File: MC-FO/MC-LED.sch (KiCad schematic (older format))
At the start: 11 parts, among them U181 TPS3703A5330DSER, U182 74ACT08SCX, U183 TPS3703A5500DSER, U184 74LVC1G07QDCKTQ1

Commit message: DSP schem, FO schem, and FO layout changes
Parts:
- R181: value 10 K -> 10K
- R182: renamed from R183; value 10 K -> 10K
- R183: renamed from R182; value 500 Ohm -> 500R
- R184: renamed from R19; value 10 K -> 10K
- renumbered U183 to U182, U182 to U183
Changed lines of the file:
@@
 Power Indicator LED CKT
 $Comp
-L Device:R_US R182
+L Device:R_US R183
 U 1 1 61706570
 P 3850 4650
-F 0 "R182" H 3700 4550 50  0000 C CNN
-F 1 "500 Ohm" H 3600 4650 50  0000 C CNN
+F 0 "R183" H 3700 4550 50  0000 C CNN
+F 1 "500R" H 3600 4650 50  0000 C CNN
 F 2 "Resistor_SMD:R_0603_1608Metric" V 3890 4640 50  0001 C CNN
 F 3 "~" H 3850 4650 50  0001 C CNN
@@
 5V
 $Comp
-L Existing_IC_Models:74ACT08SCX U182
+L Existing_IC_Models:74ACT08SCX U183
 U 1 1 6176E3CF
 P 3000 3550
-F 0 "U182" H 3000 3665 50  0000 C CNN
+F 0 "U183" H 3000 3665 50  0000 C CNN
 F 1 "74ACT08SCX" H 3000 3574 50  0000 C CNN
 F 2 "Package_SO:SOIC-14_3.9x8.7mm_P1.27mm" H 3000 3550 50  0001 C CNN
@@
 $EndComp
 $Comp
-L Existing_IC_Models:TPS3703A5500DSER U183
+L Existing_IC_Models:TPS3703A5500DSER U182
 U 1 1 6177F576
 P 4250 2250
-F 0 "U183" H 4250 2215 50  0000 C CNN
+F 0 "U182" H 4250 2215 50  0000 C CNN
 F 1 "TPS3703A5500DSER" H 4250 2124 50  0000 C CNN
 F 2 "Package_SON:WSON-6_1.5x1.5mm_P0.5mm" H 4250 2250 50  0001 C CNN
@@
 P 2900 2700
 F 0 "R181" H 2968 2746 50  0000 L CNN
-F 1 "10 K" H 2968 2655 50  0000 L CNN
+F 1 "10K" H 2968 2655 50  0000 L CNN
 F 2 "Resistor_SMD:R_0603_1608Metric" H 2900 2700 50  0001 C CNN
 F 3 "~" H 2900 2700 50  0001 C CNN
@@
 $EndComp
 $Comp
-L Device:R_Small_US R183
+L Device:R_Small_US R182
 U 1 1 617C3F20
 P 5200 2550
-F 0 "R183" H 5268 2596 50  0000 L CNN
-F 1 "10 K" H 5268 2505 50  0000 L CNN
+F 0 "R182" H 5268 2596 50  0000 L CNN
+F 1 "10K" H 5268 2505 50  0000 L CNN
 F 2 "Resistor_SMD:R_0603_1608Metric" H 5200 2550 50  0001 C CNN
 F 3 "~" H 5200 2550 50  0001 C CNN
@@
 Wire Wire Line
 	6350 4100 7050 4100
-$Comp
-L Device:R_Small_US R19
-U 1 1 6182FD38
-P 6350 3500
-F 0 "R19" H 6418 3546 50  0000 L CNN
-F 1 "10 K" H 6418 3455 50  0000 L CNN
-F 2 "Resistor_SMD:R_0603_1608Metric" H 6350 3500 50  0001 C CNN
-F 3 "~" H 6350 3500 50  0001 C CNN
-	1    6350 3500
-	1    0    0    -1
-$EndComp
 Text HLabel 6450 3100 2    50   Input ~ 0
 3V3
@@
 	0    -1   -1   0
 $EndComp
+$Comp
+L Device:R_Small_US R184
+U 1 1 6182FD38
+P 6350 3500
+F 0 "R184" H 6418 3546 50  0000 L CNN
+F 1 "10K" H 6418 3455 50  0000 L CNN
+F 2 "Resistor_SMD:R_0603_1608Metric" H 6350 3500 50  0001 C CNN
+F 3 "~" H 6350 3500 50  0001 C CNN
+	1    6350 3500
+	1    0    0    -1
+$EndComp
 $EndSCHEMATC

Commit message: Changed V-monitor circuit, V-reg circuit, finished detectors
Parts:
- removed U181: TPS3703A5330DSER, Package_SON:WSON-6_1.5x1.5mm_P0.5mm, symbol Existing_IC_Models:TPS3703A5330DSER
- removed U182: TPS3703A5500DSER, Package_SON:WSON-6_1.5x1.5mm_P0.5mm, symbol Existing_IC_Models:TPS3703A5500DSER
- added U181: BU4831F-TR, SOT130P210X105-4N, symbol BU4831F-TR:BU4831F-TR
- added U182: BU4847F-TR, SOT130P210X105-4N, symbol BU4847F-TR:BU4847F-TR
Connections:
- wire segments 87 -> 48
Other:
- moved on the sheet: C181, C182, R181, R182, U184

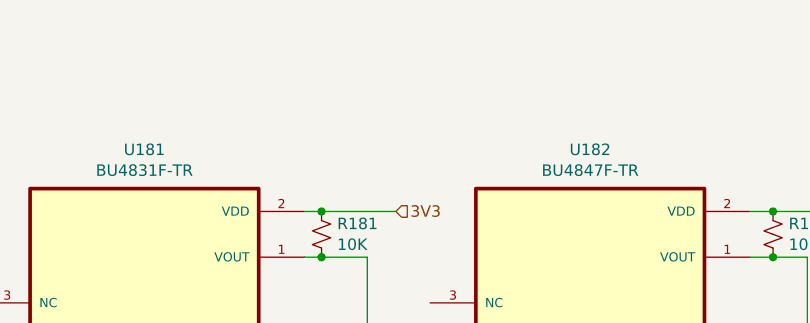
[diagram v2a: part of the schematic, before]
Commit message: updated top level of schematic with "to test" and "to do" notes
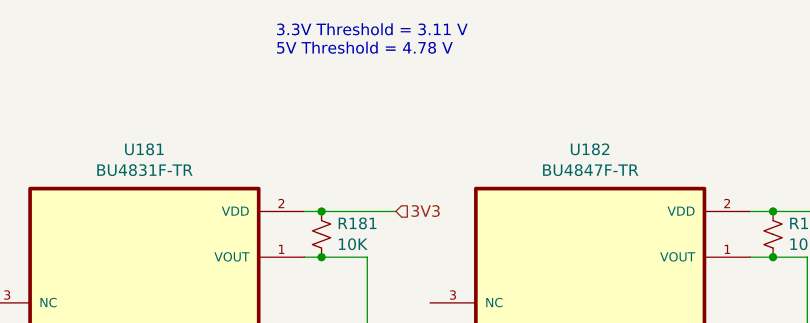
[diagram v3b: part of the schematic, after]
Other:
- note added: "3.3V Threshold = 3.11 V\n5V Threshold = 4.78 V"
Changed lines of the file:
@@
 Wire Wire Line
 	4475 3175 4475 3075
+Text Notes 3200 1400 0    50   ~ 0
+3.3V Threshold = 3.11 V\n5V Threshold = 4.78 V
 $EndSCHEMATC

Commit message: Add files via upload
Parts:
- added TP17, TP18, TP19: TestPoint, TestPoint:TestPoint_Pad_D2.0mm, symbol Connector:TestPoint
- U181, U182: footprint SOT130P210X105-4N -> Package_SO:SOP-4_3.8x4.1mm_P2.54mm
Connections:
- net 5V: no longer U183.4 (A1)
- net RESET_FO: now also U183.4 (A1), TP19.1
- net at R183.2, U183.3 (Y0), U183.8 (Y3): no longer U183.6 (Y1)
- net at U183.10 (A3), U183.11 (Y2), U183.2 (B0)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: no longer U183.5 (B1)
- net at R182.2, U182.1 (VOUT), U183.12 (B2): now also TP18.1
- net at R181.2, U181.1 (VOUT), U183.13 (A2): now also TP17.1
- new net SAFE_STATE_FLAG: U183.5 (B1), U183.6 (Y1)
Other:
- note added: "a high RESET_FO shows there are no voltage issues with FO on FO GD card. \na low RESET_FO or low Safe_state = turn off"
- note removed: "Delete status led /gpio signal"
- moved on the sheet: D181, R183
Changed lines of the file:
@@
 $Descr A4 11693 8268
 encoding utf-8
-Sheet 8 10
+Sheet 7 11
 Title ""
 Date ""
@@
 L Device:R_US R183
 U 1 1 61706570
-P 3850 4650
-F 0 "R183" H 3700 4550 50  0000 C CNN
-F 1 "500R" H 3600 4650 50  0000 C CNN
-F 2 "Resistor_SMD:R_0603_1608Metric" V 3890 4640 50  0001 C CNN
-F 3 "~" H 3850 4650 50  0001 C CNN
-	1    3850 4650
+P 3850 4500
+F 0 "R183" H 3700 4400 50  0000 C CNN
+F 1 "500R" H 3600 4500 50  0000 C CNN
+F 2 "Resistor_SMD:R_0603_1608Metric" V 3890 4490 50  0001 C CNN
+F 3 "~" H 3850 4500 50  0001 C CNN
+	1    3850 4500
 	-1   0    0    1
 $EndComp
-Text HLabel 4900 5500 3    50   Input ~ 0
-GND
-Wire Wire Line
-	3850 4300 3850 4500
+Text HLabel 4900 5250 3    50   Input ~ 0
+GND
+Wire Wire Line
+	3850 4300 3850 4350
 Wire Wire Line
 	2600 3900 2350 3900
 Wire Wire Line
-	2350 3900 2350 4200
-Wire Wire Line
-	2350 4200 2600 4200
-Wire Wire Line
-	2350 4200 2350 4550
-Wire Wire Line
 	2350 4550 3500 4550
 Wire Wire Line
@@
 Wire Wire Line
 	3500 4300 3400 4300
-Connection ~ 2350 4200
 Wire Wire Line
 	3500 4300 3850 4300
@@
 Wire Wire Line
 	3650 4700 2250 4700
-Wire Wire Line
-	2250 4700 2250 4100
 Connection ~ 3650 4100
-Wire Wire Line
-	2250 4100 2600 4100
 Text Notes 4050 7350 2    50   ~ 0
 add comparatorson both and logically AND together for LED on power status\n\n\n (windowed comparators or voltage supervisors)
-Text Notes 7700 4700 0    50   ~ 0
-Delete status led /gpio signal
 Text Notes 5800 2700 0    50   ~ 0
 if one or the other is not working pull the global reset down
-Text Notes 5900 5100 0    50   ~ 0
+Text Notes 6650 4475 0    50   ~ 0
 74LVC1G07: should be an open drain buffer\n
 Wire Wire Line
@@
 Connection ~ 6350 4100
 Wire Wire Line
-	6350 4100 7050 4100
+	6350 4100 6475 4100
 Text HLabel 6450 3100 2    50   Input ~ 0
 3V3
@@
 Wire Wire Line
 	6350 3600 6350 4100
-Text HLabel 7050 4100 2    50   Output ~ 0
-RESET_FO
 $Comp
 L Existing_IC_Models:74LVC1G07QDCKTQ1 U184
@@
 Connection ~ 6350 3100
 Wire Wire Line
-	5875 5400 4900 5400
-Wire Wire Line
-	4900 5400 4900 5500
-Wire Wire Line
-	5875 4200 5875 5400
-Wire Wire Line
-	3850 4800 3850 4900
-Wire Wire Line
-	3850 5200 3850 5400
-Wire Wire Line
-	3850 5400 4900 5400
-Connection ~ 4900 5400
+	5875 5150 4900 5150
+Wire Wire Line
+	4900 5150 4900 5250
+Wire Wire Line
+	5875 4200 5875 5150
+Wire Wire Line
+	3850 4650 3850 4750
+Wire Wire Line
+	3850 5050 3850 5150
+Wire Wire Line
+	3850 5150 4900 5150
+Connection ~ 4900 5150
 Wire Wire Line
 	3650 4100 5575 4100
-Text Notes 6150 5200 0    50   ~ 0
+Text Notes 6900 4725 0    50   ~ 0
 out of stock -- had to improvise\n
 $Comp
 L Existing_IC_Models:WP1503CB_GD D181
 U 1 1 6185A99A
-P 3750 5050
-F 0 "D181" V 3789 4832 50  0000 R CNN
-F 1 "WP1503CB_GD" V 3698 4832 50  0000 R CNN
-F 2 "Footprints_MC-FO:WP1503CBGD" H 3750 5150 50  0001 C CNN
-F 3 "" H 3750 5150 50  0001 C CNN
-	1    3750 5050
+P 3750 4900
+F 0 "D181" V 3789 4682 50  0000 R CNN
+F 1 "WP1503CB_GD" V 3698 4682 50  0000 R CNN
+F 2 "Footprints_MC-FO:WP1503CBGD" H 3750 5000 50  0001 C CNN
+F 3 "" H 3750 5000 50  0001 C CNN
+	1    3750 4900
 	0    -1   -1   0
 $EndComp
@@
 Text HLabel 2600 4300 0    50   Input ~ 0
 GND
-Connection ~ 2250 4100
-Wire Wire Line
-	2250 4100 2250 3800
 Wire Wire Line
 	2250 3800 2600 3800
@@
 Text HLabel 2600 3700 0    50   Input ~ 0
 5V
-Text HLabel 2600 4000 0    50   Input ~ 0
-5V
 Text HLabel 3400 4200 2    50   Input ~ 0
 5V
@@
 F 0 "U182" H 4575 2945 50  0000 C CNN
 F 1 "BU4847F-TR" H 4575 2854 50  0000 C CNN
-F 2 "SOT130P210X105-4N" H 4575 2375 50  0001 L BNN
+F 2 "Package_SO:SOP-4_3.8x4.1mm_P2.54mm" H 4575 2375 50  0001 L BNN
 F 3 "" H 4575 2375 50  0001 L BNN
 F 4 "Rohm" H 4575 2375 50  0001 L BNN "Manufacturer"
@@
 F 0 "U181" H 2625 2945 50  0000 C CNN
 F 1 "BU4831F-TR" H 2625 2854 50  0000 C CNN
-F 2 "SOT130P210X105-4N" H 2625 2375 50  0001 L BNN
+F 2 "Package_SO:SOP-4_3.8x4.1mm_P2.54mm" H 2625 2375 50  0001 L BNN
 F 3 "" H 2625 2375 50  0001 L BNN
 F 4 "Rohm" H 2625 2375 50  0001 L BNN "Manufacturer"
@@
 	3600 2275 3400 2275
 Wire Wire Line
-	5525 3900 5525 2275
+	5525 3900 5525 2900
 Wire Wire Line
 	5525 2275 5375 2275
@@
 	3400 2075 3725 2075
 Wire Wire Line
-	3600 3800 3600 2275
+	3600 3800 3600 2925
 Text HLabel 4025 3375 0    50   Input ~ 0
 GND
@@
 Text Notes 3200 1400 0    50   ~ 0
 3.3V Threshold = 3.11 V\n5V Threshold = 4.78 V
+Wire Wire Line
+	2350 3900 2350 4550
+Wire Wire Line
+	2250 3800 2250 4700
+Wire Wire Line
+	6475 4100 6475 5275
+Wire Wire Line
+	6475 5550 1775 5550
+Wire Wire Line
+	1775 5550 1775 4000
+Wire Wire Line
+	1775 4000 2600 4000
+Text Label 1775 4000 0    50   ~ 0
+RESET_FO
+Text HLabel 1475 4200 0    50   BiDi ~ 0
+SAFE_STATE_FLAG
+Wire Wire Line
+	1475 4200 1975 4200
+Wire Wire Line
+	2600 4100 1975 4100
+Wire Wire Line
+	1975 4100 1975 4200
+Connection ~ 1975 4200
+Wire Wire Line
+	1975 4200 2600 4200
+Text Notes 7100 900  0    50   ~ 0
+a high RESET_FO shows there are no voltage issues with FO on FO GD card. \na low RESET_FO or low Safe_state = turn off
+Text Label 6450 4100 0    50   ~ 0
+RESET_FO
+$Comp
+L Connector:TestPoint TP19
+U 1 1 623DE1C7
+P 6475 5275
+F 0 "TP19" V 6429 5463 50  0000 L CNN
+F 1 "TestPoint" V 6520 5463 50  0000 L CNN
+F 2 "TestPoint:TestPoint_Pad_D2.0mm" H 6675 5275 50  0001 C CNN
+F 3 "~" H 6675 5275 50  0001 C CNN
+	1    6475 5275
+	0    1    1    0
+$EndComp
+Connection ~ 6475 5275
+Wire Wire Line
+	6475 5275 6475 5550
+$Comp
+L Connector:TestPoint TP17
+U 1 1 623DFD90
+P 3600 2925
+F 0 "TP17" V 3554 3113 50  0000 L CNN
+F 1 "TestPoint" V 3645 3113 50  0000 L CNN
+F 2 "TestPoint:TestPoint_Pad_D2.0mm" H 3800 2925 50  0001 C CNN
+F 3 "~" H 3800 2925 50  0001 C CNN
+	1    3600 2925
+	0    1    1    0
+$EndComp
+Connection ~ 3600 2925
+Wire Wire Line
+	3600 2925 3600 2275
+$Comp
+L Connector:TestPoint TP18
+U 1 1 623E05CE
+P 5525 2900
+F 0 "TP18" V 5479 3088 50  0000 L CNN
+F 1 "TestPoint" V 5570 3088 50  0000 L CNN
+F 2 "TestPoint:TestPoint_Pad_D2.0mm" H 5725 2900 50  0001 C CNN
+F 3 "~" H 5725 2900 50  0001 C CNN
+	1    5525 2900
+	0    1    1    0
+$EndComp
+Connection ~ 5525 2900
+Wire Wire Line
+	5525 2900 5525 2275
 $EndSCHEMATC

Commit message: updating SAFE_STATE_FLAG and EMITTER_ENABLE
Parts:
- removed D181: WP1503CB_GD, Footprints_MC-FO:WP1503CBGD, symbol Existing_IC_Models:WP1503CB_GD
- removed R183: 500R, Resistor_SMD:R_0603_1608Metric, symbol Device:R_US
- removed TP19: TestPoint, TestPoint:TestPoint_Pad_D2.0mm, symbol Connector:TestPoint
- added D?: WP1503CB_GD, Footprints_MC-FO:WP1503CBGD, symbol Existing_IC_Models:WP1503CB_GD
- added R?: 500R, Resistor_SMD:R_0603_1608Metric, symbol Device:R_US
- added R?: 10K, Resistor_SMD:R_0603_1608Metric, symbol Device:R_Small_US
- added TP?: TestPoint, TestPoint:TestPoint_Pad_D2.0mm, symbol Connector:TestPoint
- added U?: 74LVC1G07QDCKTQ1, Package_TO_SOT_SMD:SOT-353_SC-70-5, symbol Existing_IC_Models:74LVC1G07QDCKTQ1
- added U?: 74LVCE1G08W5-7, symbol MC-FO:74LVCE1G08W5-7
- U181: symbol BU4831F-TR:BU4831F-TR -> MC-FO:BU4831F-TR
- U182: symbol BU4847F-TR:BU4847F-TR -> MC-FO:BU4847F-TR
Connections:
- net labels added: ~RESET_FO~, ~SAFE_STATE_FLAG~
- net labels removed: RESET_FO, SAFE_STATE_FLAG
- wire segments 55 -> 67
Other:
- note added: "Safe_state_flag is like a global reset to connector and to\n all transcievers. pulled low if any voltage issues on this \ncard or any other card. can also be pulled low by dsp"
- note added: "a high ~RESET_FO~ shows there are no voltage issues with FO on FO GD card. \na low RESET_FO or low Safe_state = turn off"
- note removed: "a high RESET_FO shows there are no voltage issues with FO on FO GD card. \na low RESET_FO or low Safe_state = turn off"
- note removed: "out of stock -- had to improvise\n"
- note removed: "reset to connector and to all transcievers"
- moved on the sheet: C181, C182, R181, R182, R184, TP17, TP18, U183, U184

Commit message: schematic changes--> layout rev
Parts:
- removed R?: 10K, Resistor_SMD:R_0603_1608Metric, symbol Device:R_Small_US
- removed U183: 74ACT08SCX, Package_SO:SOIC-14_3.9x8.7mm_P1.27mm, symbol Existing_IC_Models:74ACT08SCX
- removed U?: 74LVC1G07QDCKTQ1, Package_TO_SOT_SMD:SOT-353_SC-70-5, symbol Existing_IC_Models:74LVC1G07QDCKTQ1
- U181: renamed from U184; footprint Package_TO_SOT_SMD:SOT-353_SC-70-5 -> Package_TO_SOT_SMD:SOT-353_SC-70-5_Handsoldering
- U182: renamed from U?; footprint (none) -> Package_TO_SOT_SMD:SOT-23-5_HandSoldering
- gave numbers to parts that had none: 3
- renumbered C182 to C181, C181 to C182, R184 to R182, R181 to R184, R182 to R185, TP17 to TP182, TP18 to TP183, U181 to U183, U182 to U184
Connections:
- net labels removed: ~RESET_FO~
- wire segments 67 -> 36
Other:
- note removed: "a high ~RESET_FO~ shows there are no voltage issues with FO on FO GD card. \na low RESET_FO or low Safe_state = turn off"
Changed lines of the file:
@@
 Text HLabel 3125 4125 0    50   Input ~ 0
 GND
-Wire Wire Line
-	4975 10150 4725 10150
-Wire Wire Line
-	4725 10800 5875 10800
-Wire Wire Line
-	5875 10800 5875 10550
-Wire Wire Line
-	5875 10550 5775 10550
-Wire Wire Line
-	5875 10550 6225 10550
-Connection ~ 5875 10550
-Wire Wire Line
-	6025 10250 6025 10350
-Wire Wire Line
-	5775 10250 6025 10250
-Wire Wire Line
-	5775 10350 6025 10350
-Wire Wire Line
-	6025 10350 6025 10950
-Wire Wire Line
-	6025 10950 4625 10950
-Connection ~ 6025 10350
 Text Notes 4050 7350 2    50   ~ 0
 add comparatorson both and logically AND together for LED on power status\n\n\n (windowed comparators or voltage supervisors)
@@
 	2825 2925 2825 3225
 $Comp
-L Existing_IC_Models:74LVC1G07QDCKTQ1 U184
+L Existing_IC_Models:74LVC1G07QDCKTQ1 U181
 U 1 1 617E8424
 P 3125 3925
-F 0 "U184" H 2975 4175 50  0000 C CNN
+F 0 "U181" H 2975 4175 50  0000 C CNN
 F 1 "74LVC1G07QDCKTQ1" H 2725 4075 50  0000 C CNN
-F 2 "Package_TO_SOT_SMD:SOT-353_SC-70-5" H 3125 3925 50  0001 C CNN
-F 3 "http://www.ti.com/lit/sg/scyt129e/scyt129e.pdf" H 3125 3925 50  0001 C CNN
+F 2 "Package_TO_SOT_SMD:SOT-353_SC-70-5_Handsoldering" H 3125 3925 50  0001 C CNN
+F 3 "https://www.ti.com/lit/ds/symlink/sn74lvc1g07-q1.pdf?HQS=dis-mous-null-mousermode-dsf-pf-null-wwe&ts=1646082303416&ref_url=https%253A%252F%252Fwww.mouser.com%252F" H 3125 3925 50  0001 C CNN
 	1    3125 3925
 	-1   0    0    -1
@@
 Wire Wire Line
 	3125 4025 3125 4125
-Wire Wire Line
-	6025 10350 7950 10350
-$Comp
-L Device:R_Small_US R184
+$Comp
+L Device:R_Small_US R182
 U 1 1 6182FD38
 P 2825 3325
-F 0 "R184" H 2893 3371 50  0000 L CNN
+F 0 "R182" H 2893 3371 50  0000 L CNN
 F 1 "10K" H 2893 3280 50  0000 L CNN
 F 2 "Resistor_SMD:R_0603_1608Metric" H 2825 3325 50  0001 C CNN
@@
 	-1   0    0    -1
 $EndComp
-Text HLabel 4975 10550 0    50   Input ~ 0
-GND
-Wire Wire Line
-	4625 10050 4975 10050
 Text HLabel 5825 3075 2    50   Input ~ 0
 GND
 $Comp
-L Device:R_Small_US R182
+L Device:R_Small_US R185
 U 1 1 617C3F20
 P 7875 2575
-F 0 "R182" H 7943 2621 50  0000 L CNN
+F 0 "R185" H 7943 2621 50  0000 L CNN
 F 1 "10K" H 7943 2530 50  0000 L CNN
 F 2 "Resistor_SMD:R_0603_1608Metric" H 7875 2575 50  0001 C CNN
@@
 $EndComp
 $Comp
-L Device:R_Small_US R181
+L Device:R_Small_US R184
 U 1 1 617C2D42
 P 6100 2575
-F 0 "R181" H 6168 2621 50  0000 L CNN
+F 0 "R184" H 6168 2621 50  0000 L CNN
 F 1 "10K" H 6168 2530 50  0000 L CNN
 F 2 "Resistor_SMD:R_0603_1608Metric" H 6100 2575 50  0001 C CNN
@@
 5V
 $Comp
-L Device:C_Small C181
+L Device:C_Small C182
 U 1 1 617CFF8B
 P 2600 2125
-F 0 "C181" H 2692 2171 50  0000 L CNN
+F 0 "C182" H 2692 2171 50  0000 L CNN
 F 1 "1 uF or unpop" H 2692 2080 50  0000 L CNN
 F 2 "Capacitor_SMD:C_0603_1608Metric" H 2600 2125 50  0001 C CNN
@@
 $EndComp
 $Comp
-L Device:C_Small C182
+L Device:C_Small C181
 U 1 1 617D05D8
 P 2225 2125
-F 0 "C182" H 2317 2171 50  0000 L CNN
+F 0 "C181" H 2317 2171 50  0000 L CNN
 F 1 "1 uF" H 2317 2080 50  0000 L CNN
 F 2 "Capacitor_SMD:C_0603_1608Metric" H 2225 2125 50  0001 C CNN
@@
 $EndComp
 $Comp
-L Existing_IC_Models:74ACT08SCX U183
-U 1 1 6176E3CF
-P 5375 9800
-F 0 "U183" H 5375 9915 50  0000 C CNN
-F 1 "74ACT08SCX" H 5375 9824 50  0000 C CNN
-F 2 "Package_SO:SOIC-14_3.9x8.7mm_P1.27mm" H 5375 9800 50  0001 C CNN
-F 3 "" H 5375 9800 50  0001 C CNN
-	1    5375 9800
-	1    0    0    -1
-$EndComp
-Text HLabel 4975 9950 0    50   Input ~ 0
-5V
-$Comp
-L MC-FO:BU4847F-TR U182
+L MC-FO:BU4847F-TR U184
 U 1 1 61A5F13F
 P 7075 2775
-F 0 "U182" H 7075 3345 50  0000 C CNN
+F 0 "U184" H 7075 3345 50  0000 C CNN
 F 1 "BU4847F-TR" H 7075 3254 50  0000 C CNN
 F 2 "Package_SO:SOP-4_3.8x4.1mm_P2.54mm" H 7075 2775 50  0001 L BNN
-F 3 "" H 7075 2775 50  0001 L BNN
+F 3 "https://fscdn.rohm.com/en/products/databook/datasheet/ic/power/voltage_detector/bu48xxg-e.pdf" H 7075 2775 50  0001 L BNN
 F 4 "Rohm" H 7075 2775 50  0001 L BNN "Manufacturer"
 F 5 "SOT130P210X105-4N" H 7075 2775 50  0001 L BNN "Package"
@@
 $EndComp
 $Comp
-L MC-FO:BU4831F-TR U181
+L MC-FO:BU4831F-TR U183
 U 1 1 61A601DB
 P 5125 2775
-F 0 "U181" H 5125 3345 50  0000 C CNN
+F 0 "U183" H 5125 3345 50  0000 C CNN
 F 1 "BU4831F-TR" H 5125 3254 50  0000 C CNN
 F 2 "Package_SO:SOP-4_3.8x4.1mm_P2.54mm" H 5125 2775 50  0001 L BNN
-F 3 "" H 5125 2775 50  0001 L BNN
+F 3 "https://fscdn.rohm.com/en/products/databook/datasheet/ic/power/voltage_detector/bu48xxg-e.pdf" H 5125 2775 50  0001 L BNN
 F 4 "Rohm" H 5125 2775 50  0001 L BNN "Manufacturer"
 F 5 "SOT130P210X105-4N" H 5125 2775 50  0001 L BNN "Package"
@@
 	1    0    0    -1
 $EndComp
-Text HLabel 5775 9950 2    50   Input ~ 0
-5V
-Wire Wire Line
-	5775 10050 5975 10050
 Wire Wire Line
 	8025 2675 7875 2675
-Wire Wire Line
-	5775 10150 7900 10150
 Text HLabel 7775 3075 2    50   Input ~ 0
 GND
@@
 Wire Wire Line
 	6100 2475 6100 2375
-Wire Wire Line
-	5975 10050 5975 9175
 Text HLabel 2150 2225 0    50   Input ~ 0
 GND
@@
 Text Notes 5800 2000 0    50   ~ 0
 3.3V Threshold = 3.11 V\n5V Threshold = 4.78 V
-Wire Wire Line
-	4725 10150 4725 10800
-Wire Wire Line
-	4625 10050 4625 10950
-Wire Wire Line
-	8850 11800 4150 11800
-Wire Wire Line
-	4150 11800 4150 10250
-Wire Wire Line
-	4150 10250 4975 10250
-Text Label 4150 10250 0    50   ~ 0
-~RESET_FO~
-Text HLabel 2250 10350 0    50   BiDi ~ 0
-~SAFE_STATE_FLAG~
-Text Notes 950  750  0    50   ~ 0
-a high ~RESET_FO~ shows there are no voltage issues with FO on FO GD card. \na low RESET_FO or low Safe_state = turn off
-$Comp
-L Connector:TestPoint TP17
+$Comp
+L Connector:TestPoint TP182
 U 1 1 623DFD90
 P 6100 3325
-F 0 "TP17" V 6054 3513 50  0000 L CNN
+F 0 "TP182" V 6054 3513 50  0000 L CNN
 F 1 "TestPoint" V 6145 3513 50  0000 L CNN
 F 2 "TestPoint:TestPoint_Pad_D2.0mm" H 6300 3325 50  0001 C CNN
@@
 	6100 3325 6100 2675
 $Comp
-L Connector:TestPoint TP18
+L Connector:TestPoint TP183
 U 1 1 623E05CE
 P 8025 3300
-F 0 "TP18" V 7979 3488 50  0000 L CNN
+F 0 "TP183" V 7979 3488 50  0000 L CNN
 F 1 "TestPoint" V 8070 3488 50  0000 L CNN
 F 2 "TestPoint:TestPoint_Pad_D2.0mm" H 8225 3300 50  0001 C CNN
@@
 5V
 Wire Wire Line
-	3850 10450 4975 10450
-Wire Wire Line
-	3850 10450 3850 10725
-Wire Wire Line
-	3850 10725 3200 10725
-$Comp
-L Existing_IC_Models:74LVC1G07QDCKTQ1 U?
-U 1 1 621B8DE3
-P 2900 10725
-F 0 "U?" H 2750 10975 50  0000 C CNN
-F 1 "74LVC1G07QDCKTQ1" H 2500 10875 50  0000 C CNN
-F 2 "Package_TO_SOT_SMD:SOT-353_SC-70-5" H 2900 10725 50  0001 C CNN
-F 3 "http://www.ti.com/lit/sg/scyt129e/scyt129e.pdf" H 2900 10725 50  0001 C CNN
-	1    2900 10725
-	-1   0    0    -1
-$EndComp
-Wire Wire Line
-	2250 10350 2475 10350
-Wire Wire Line
-	2650 10725 2475 10725
-Wire Wire Line
-	2475 10725 2475 10350
-Connection ~ 2475 10350
-Wire Wire Line
-	2475 10350 4975 10350
-Wire Wire Line
-	2900 10625 2900 9925
-Wire Wire Line
-	2900 9925 3200 9925
-Text HLabel 3200 9925 2    50   Input ~ 0
-3V3
-Wire Wire Line
-	2900 10825 2900 11125
-Wire Wire Line
-	2900 11125 2825 11125
-Text HLabel 2825 11125 0    50   Input ~ 0
-GND
-Wire Wire Line
 	6275 2375 6100 2375
 Wire Wire Line
@@
 Connection ~ 6100 3325
 $Comp
-L MC-FO:74LVCE1G08W5-7 U?
+L MC-FO:74LVCE1G08W5-7 U182
 U 1 1 6222C302
 P 4625 3925
-F 0 "U?" H 4600 4192 50  0000 C CNN
+F 0 "U182" H 4600 4192 50  0000 C CNN
 F 1 "74LVCE1G08W5-7" H 4600 4101 50  0000 C CNN
-F 2 "" H 4625 3925 50  0001 C CNN
+F 2 "Package_TO_SOT_SMD:SOT-23-5_HandSoldering" H 4625 3925 50  0001 C CNN
 F 3 "https://www.diodes.com/assets/Datasheets/74LVCE1G08.pdf" H 4625 3925 50  0001 C CNN
 	1    4625 3925
@@
 GND
 $Comp
-L Device:R_US R?
+L Device:R_US R183
 U 1 1 62237A0E
 P 3950 4675
-F 0 "R?" H 3800 4575 50  0000 C CNN
+F 0 "R183" H 3800 4575 50  0000 C CNN
 F 1 "500R" H 3700 4675 50  0000 C CNN
 F 2 "Resistor_SMD:R_0603_1608Metric" V 3990 4665 50  0001 C CNN
@@
 	3950 4825 3950 4925
 $Comp
-L Existing_IC_Models:WP1503CB_GD D?
+L Existing_IC_Models:WP1503CB_GD D181
 U 1 1 62237A18
 P 3850 5075
-F 0 "D?" V 3889 4857 50  0000 R CNN
+F 0 "D181" V 3889 4857 50  0000 R CNN
 F 1 "WP1503CB_GD" V 3798 4857 50  0000 R CNN
 F 2 "Footprints_MC-FO:WP1503CBGD" H 3850 5175 50  0001 C CNN
@@
 ~SAFE_STATE_FLAG~
 $Comp
-L Connector:TestPoint TP?
+L Connector:TestPoint TP181
 U 1 1 622717CC
 P 2175 3925
-F 0 "TP?" V 2129 4113 50  0000 L CNN
+F 0 "TP181" V 2129 4113 50  0000 L CNN
 F 1 "TestPoint" V 2220 4113 50  0000 L CNN
 F 2 "TestPoint:TestPoint_Pad_D2.0mm" H 2375 3925 50  0001 C CNN
@@
 Wire Wire Line
 	2175 3925 1750 3925
-$Comp
-L Device:R_Small_US R?
-U 1 1 62333FCA
-P 2725 -500
-F 0 "R?" H 2793 -454 50  0000 L CNN
-F 1 "10K" H 2793 -545 50  0000 L CNN
-F 2 "Resistor_SMD:R_0603_1608Metric" H 2725 -500 50  0001 C CNN
-F 3 "~" H 2725 -500 50  0001 C CNN
-	1    2725 -500
-	-1   0    0    -1
-$EndComp
 $EndSCHEMATC
